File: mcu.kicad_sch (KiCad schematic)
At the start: 0 parts

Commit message: add decoupling pins
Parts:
- added C24, C25, C26: 2.2uF, symbol Device:C
- added U3: STM32F733VETx, Package_QFP:LQFP-100_14x14mm_P0.5mm, symbol MCU_ST_STM32F7:STM32F733VETx
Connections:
- new net: C24.1, U3.48 (VCAP_1)
- new net: C26.1, U3.54 (VDDPHYHS)
- new net: C25.1, U3.73 (VCAP_2)
- new net +3.3V: U3.100 (VDD), U3.11 (VDD), U3.27 (VDD), U3.50 (VDD), U3.6 (VBAT), U3.75 (VDD)
- new net +3.3VA: U3.20 (VREF+), U3.21 (VDDA)
- new net GND: C24.2, C25.2, C26.2, U3.10 (VSS), U3.26 (VSS), U3.49 (VSS), U3.74 (VSS), U3.99 (VSS)
- new net GNDA: U3.19 (VSSA)

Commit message: finish power caps
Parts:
- added C28: 100nF, symbol Device:C
- added C29: 1uF, symbol Device:C
- added C30: 2.2uF, symbol Device:C
- added R4: 10k, symbol Device:R
- added R5: 3k, symbol Device:R
- added SW1: SW_Omron_B3FS, symbol Switch:SW_Omron_B3FS
- C26: value 2.2uF -> 100nF
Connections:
- net +3.3V: now also U3.94 (BOOT0), R4.1
- net +3.3VA: no longer U3.20 (VREF+)
- net GND: now also C28.2, C29.2, C30.2, R4.2, R5.2, SW1.1
- net NRST: now reaches U3.14 (NRST)
- net NRST: now also C26.1, SW1.2
- net REXTPHYHS: now reaches U3.53 (REXTPHYHS)
- net REXTPHYHS: now also R5.1
- net +3.3VUSB: now reaches U3.54 (VDDPHYHS)
- net +3.3VUSB: no longer C26.1
- net V12PHYHS: now reaches U3.55 (V12PHYHS)
- net V12PHYHS: now also C30.1
- new net VREF+: C28.1, C29.1, U3.20 (VREF+)
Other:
- note added: "MISC PINS"

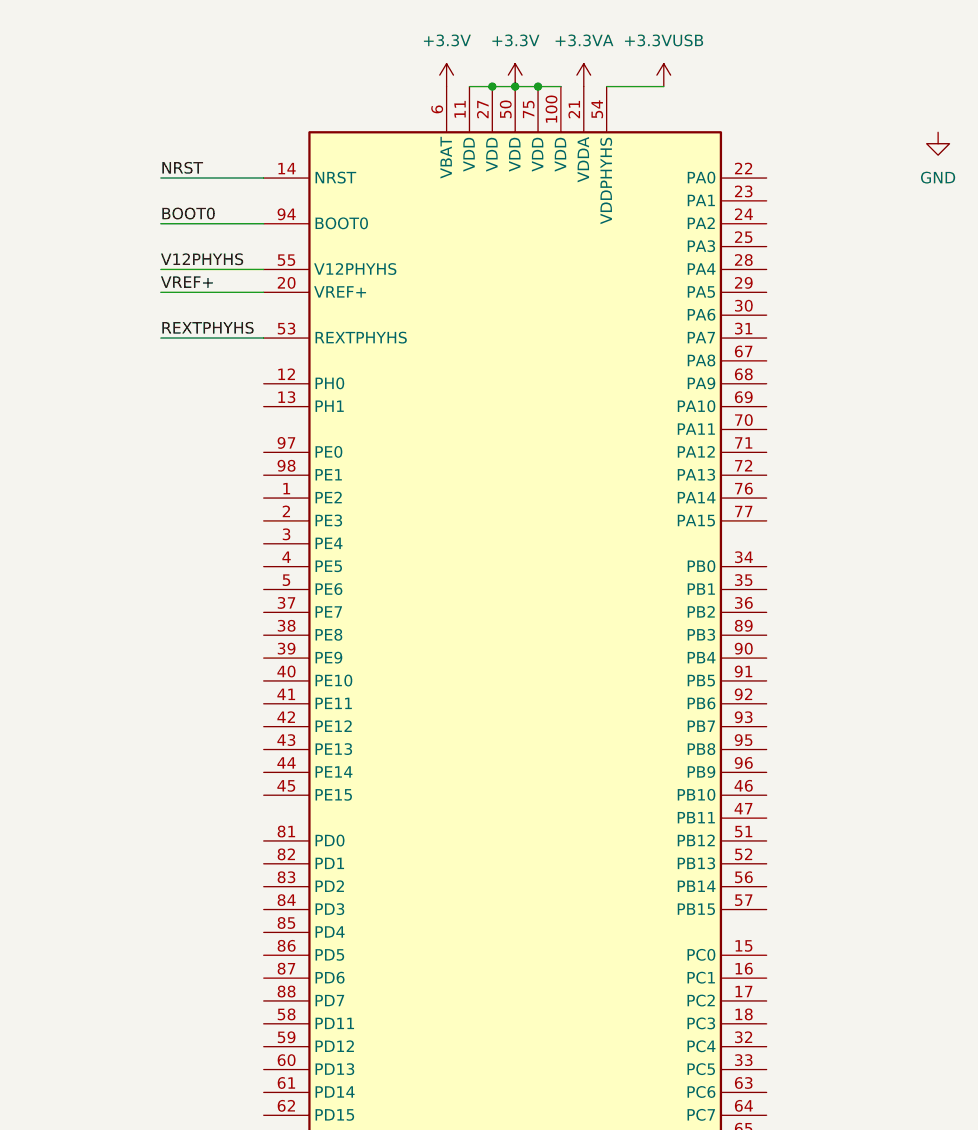
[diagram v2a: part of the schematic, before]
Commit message: add sensors and muxes
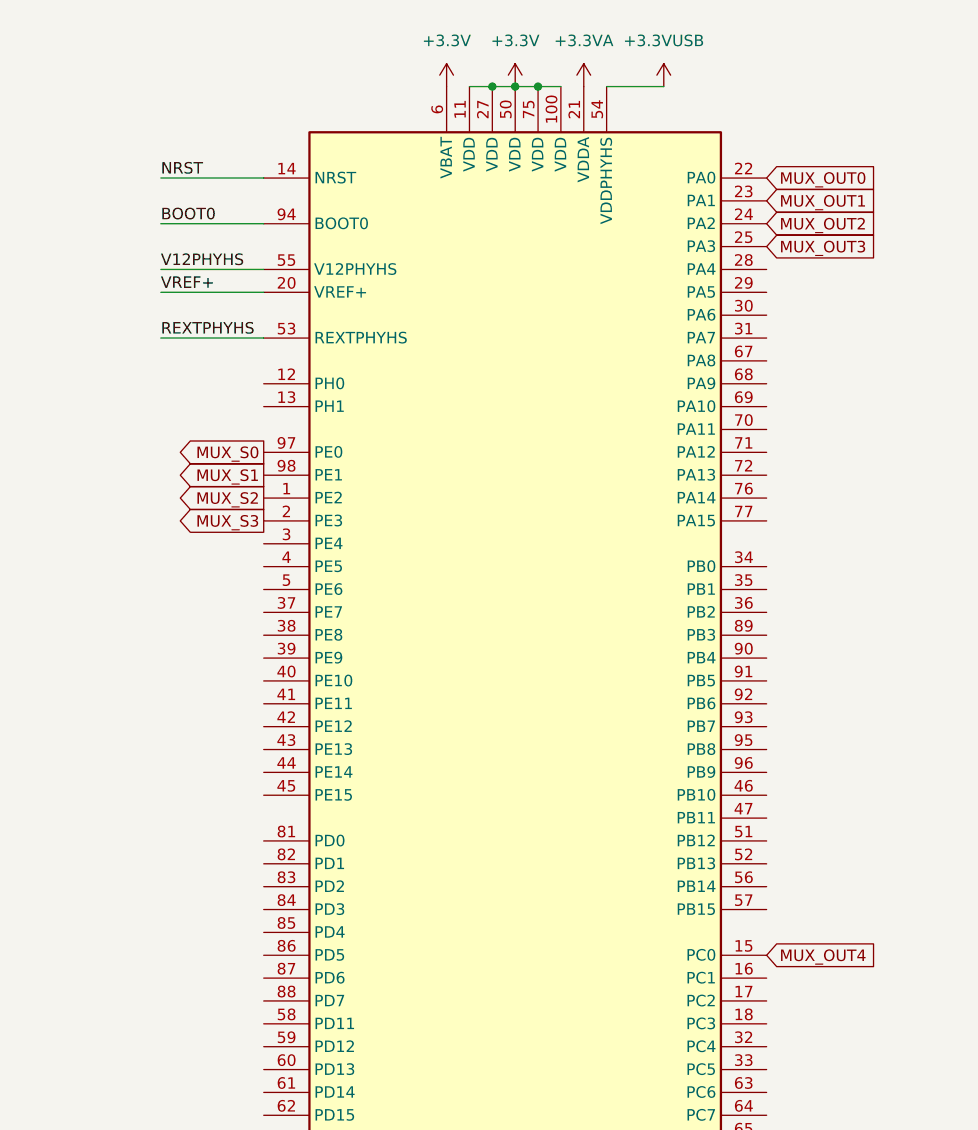
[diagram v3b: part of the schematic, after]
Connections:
- net MUX_S2: now reaches U3.1 (PE2)
- net MUX_OUT4: now reaches U3.15 (PC0)
- net MUX_S3: now reaches U3.2 (PE3)
- net MUX_OUT0: now reaches U3.22 (PA0)
- net MUX_OUT1: now reaches U3.23 (PA1)
- net MUX_OUT2: now reaches U3.24 (PA2)
- net MUX_OUT3: now reaches U3.25 (PA3)
- net MUX_S0: now reaches U3.97 (PE0)
- net MUX_S1: now reaches U3.98 (PE1)
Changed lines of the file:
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@@
+		)
+	)
+	(global_label "MUX_S2"
+		(shape output)
+		(at 119.38 71.12 180)
+		(fields_autoplaced yes)
+		(effects
+			(font
+				(size 1.27 1.27)
+			)
+			(justify right)
+		)
+		(property "Intersheetrefs" "${INTERSHEET_REFS}"
+			(at 109.0168 71.12 0)
+			(hide yes)
+			(show_name no)
+			(do_not_autoplace no)
+			(effects
+				(font
+					(size 1.27 1.27)
+				)
+				(justify right)
+			)
+		)
+	)
+	(global_label "MUX_OUT2"
+		(shape input)
+		(at 175.26 40.64 0)
+		(fields_autoplaced yes)
+		(effects
+			(font
+				(size 1.27 1.27)
+			)
+			(justify left)
+		)
+		(property "Intersheetrefs" "${INTERSHEET_REFS}"
+			(at 188.0423 40.64 0)
+			(hide yes)
+			(show_name no)
+			(do_not_autoplace no)
+			(effects
+				(font
+					(size 1.27 1.27)
+				)
+				(justify left)
+			)
+		)
+	)
+	(global_label "MUX_S0"
+		(shape output)
+		(at 119.38 66.04 180)
+		(fields_autoplaced yes)
+		(effects
+			(font
+				(size 1.27 1.27)
+			)
+			(justify right)
+		)
+		(property "Intersheetrefs" "${INTERSHEET_REFS}"
+			(at 109.0168 66.04 0)
+			(hide yes)
+			(show_name no)
+			(do_not_autoplace no)
+			(effects
+				(font
+					(size 1.27 1.27)
+				)
+				(justify right)
+			)
+		)
+	)
+	(global_label "MUX_S1"
+		(shape output)
+		(at 119.38 68.58 180)
+		(fields_autoplaced yes)
+		(effects
+			(font
+				(size 1.27 1.27)
+			)
+			(justify right)
+		)
+		(property "Intersheetrefs" "${INTERSHEET_REFS}"
+			(at 109.0168 68.58 0)
+			(hide yes)
+			(show_name no)
+			(do_not_autoplace no)
+			(effects
+				(font
+					(size 1.27 1.27)
+				)
+				(justify right)
+			)
+		)
+	)
+	(global_label "MUX_OUT4"
+		(shape input)
+		(at 175.26 121.92 0)
+		(fields_autoplaced yes)
+		(effects
+			(font
+				(size 1.27 1.27)
+			)
+			(justify left)
+		)
+		(property "Intersheetrefs" "${INTERSHEET_REFS}"
+			(at 188.0423 121.92 0)
+			(hide yes)
+			(show_name no)
+			(do_not_autoplace no)
+			(effects
+				(font
+					(size 1.27 1.27)
+				)
+				(justify left)
+			)
+		)
+	)
+	(global_label "MUX_OUT0"
+		(shape input)
+		(at 175.26 35.56 0)
+		(fields_autoplaced yes)
+		(effects
+			(font
+				(size 1.27 1.27)
+			)
+			(justify left)
+		)
+		(property "Intersheetrefs" "${INTERSHEET_REFS}"
+			(at 188.0423 35.56 0)
+			(hide yes)
+			(show_name no)
+			(do_not_autoplace no)
+			(effects
+				(font
+					(size 1.27 1.27)
+				)
+				(justify left)
+			)
+		)
+	)
+	(global_label "MUX_OUT1"
+		(shape input)
+		(at 175.26 38.1 0)
+		(fields_autoplaced yes)
+		(effects
+			(font
+				(size 1.27 1.27)
+			)
+			(justify left)
+		)
+		(property "Intersheetrefs" "${INTERSHEET_REFS}"
+			(at 188.0423 38.1 0)
+			(hide yes)
+			(show_name no)
+			(do_not_autoplace no)
+			(effects
+				(font
+					(size 1.27 1.27)
+				)
+				(justify left)
+			)
+		)
+	)
+	(global_label "MUX_S3"
+		(shape output)
+		(at 119.38 73.66 180)
+		(fields_autoplaced yes)
+		(effects
+			(font
+				(size 1.27 1.27)
+			)
+			(justify right)
+		)
+		(property "Intersheetrefs" "${INTERSHEET_REFS}"
+			(at 109.0168 73.66 0)
+			(hide yes)
+			(show_name no)
+			(do_not_autoplace no)
+			(effects
+				(font
+					(size 1.27 1.27)
+				)
+				(justify right)
+			)
+		)
+	)
+	(global_label "MUX_OUT3"
+		(shape input)
+		(at 175.26 43.18 0)
+		(fields_autoplaced yes)
+		(effects
+			(font
+				(size 1.27 1.27)
+			)
+			(justify left)
+		)
+		(property "Intersheetrefs" "${INTERSHEET_REFS}"
+			(at 188.0423 43.18 0)
+			(hide yes)
+			(show_name no)
+			(do_not_autoplace no)
+			(effects
+				(font
+					(size 1.27 1.27)
+				)
+				(justify left)
+			)
 		)
 	)
@@
 					(unit 1)
 				)
-			)
-		)
-	)
-	(symbol
-		(lib_id "power:GND")
-		(at 194.31 30.48 0)
-		(unit 1)
-		(body_style 1)
-		(exclude_from_sim no)
-		(in_bom yes)
-		(on_board yes)
-		(in_pos_files yes)
-		(dnp no)
-		(fields_autoplaced yes)
-		(property "Reference" "#PWR043"
-			(at 194.31 36.83 0)
-			(hide yes)
-			(show_name no)
-			(do_not_autoplace no)
-			(effects
-				(font
-					(size 1.27 1.27)
-				)
-			)
-		)
-		(property "Value" "GND"
-			(at 194.31 35.56 0)
-			(show_name no)
-			(do_not_autoplace no)
-			(effects
-				(font
-					(size 1.27 1.27)
-				)
-			)
-		)
-		(property "Footprint" ""
-			(at 194.31 30.48 0)
-			(hide yes)
-			(show_name no)
-			(do_not_autoplace no)
-			(effects
-				(font
-					(size 1.27 1.27)
-				)
-			)
-		)
-		(property "Datasheet" ""
-			(at 194.31 30.48 0)
-			(hide yes)
-			(show_name no)
-			(do_not_autoplace no)
-			(effects
-				(font
-					(size 1.27 1.27)
-				)
-			)
-		)
-		(property "Description" "Power symbol creates a global label with name \"GND\" , ground"
-			(at 194.31 30.48 0)
-			(hide yes)
-			(show_name no)
-			(do_not_autoplace no)
-			(effects
-				(font
-					(size 1.27 1.27)
-				)
-			)
-		)
-		(pin "1"
-		)
-		(instances
-			(project "makeyboard"
-				(path "/fdf51568-632f-4761-8398-b51798d1e133/09615ad3-ae97-45a3-ad21-d8d1fc65895c"
-					(reference "#PWR043")
-					(unit 1)
-				)
